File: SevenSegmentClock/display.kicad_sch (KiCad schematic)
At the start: 104 parts, among them Q1 PN2222A, Q2 PN2222A, Q3 PN2222A, Q4 PN2222A, Q5 PN2222A, Q6 PN2222A, Q7 13N50F, U1 4511, U10 4042, U11 4511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

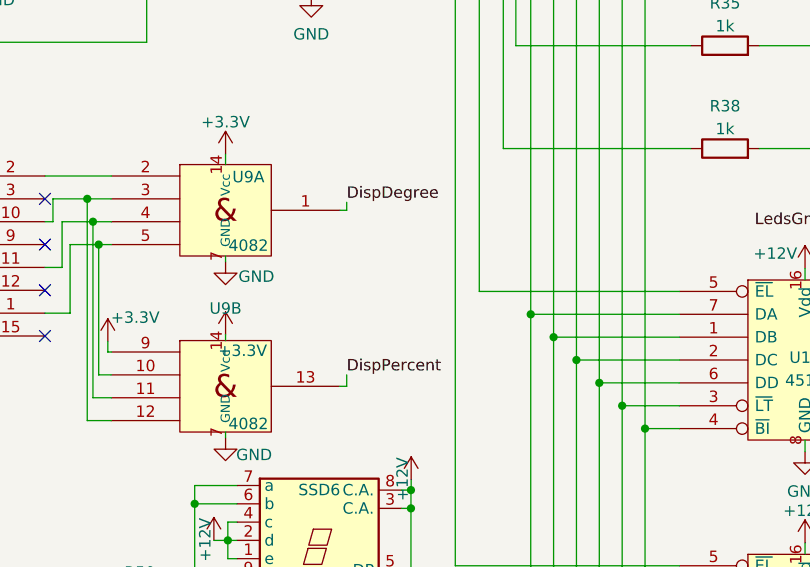
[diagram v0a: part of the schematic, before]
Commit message: Swapping around percentage and degree indicators
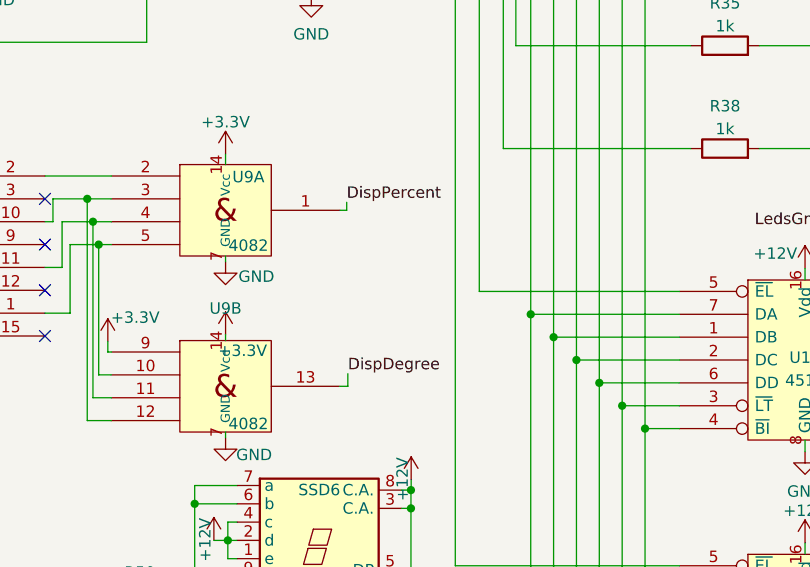
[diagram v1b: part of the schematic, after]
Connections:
- net DispDegree: now also U9.13; no longer U9.1
- net DispPercent: now also U9.1; no longer U9.13
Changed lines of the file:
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@@
-    (stroke (width 0) (type default))
-  )
-  (wire (pts (xy 91.059 203.581) (xy 91.059 202.311))
     (stroke (width 0) (type default))
   )
@@
     (stroke (width 0) (type default))
   )
+  (wire (pts (xy 91.186 203.581) (xy 91.186 202.184))
+    (stroke (width 0) (type default))
+  )
   (wire (pts (xy 114.046 25.4) (xy 114.046 57.15))
     (stroke (width 0) (type default))
@@
     (stroke (width 0) (type default))
   )
-  (wire (pts (xy 90.297 203.581) (xy 91.059 203.581))
+  (wire (pts (xy 90.297 203.581) (xy 91.186 203.581))
     (stroke (width 0) (type default))
   )
@@
     (effects (font (size 1.27 1.27)) (justify right bottom))
   )
-  (label "DispPercent" (at 91.059 202.311 0) (fields_autoplaced)
+  (label "DispPercent" (at 91.059 183.134 0) (fields_autoplaced)
     (effects (font (size 1.27 1.27)) (justify left bottom))
   )
@@
     (effects (font (size 1.27 1.27)) (justify right bottom))
   )
-  (label "DispDegree" (at 91.059 183.134 0) (fields_autoplaced)
+  (label "DispDegree" (at 91.186 202.184 0) (fields_autoplaced)
     (effects (font (size 1.27 1.27)) (justify left bottom))
   )

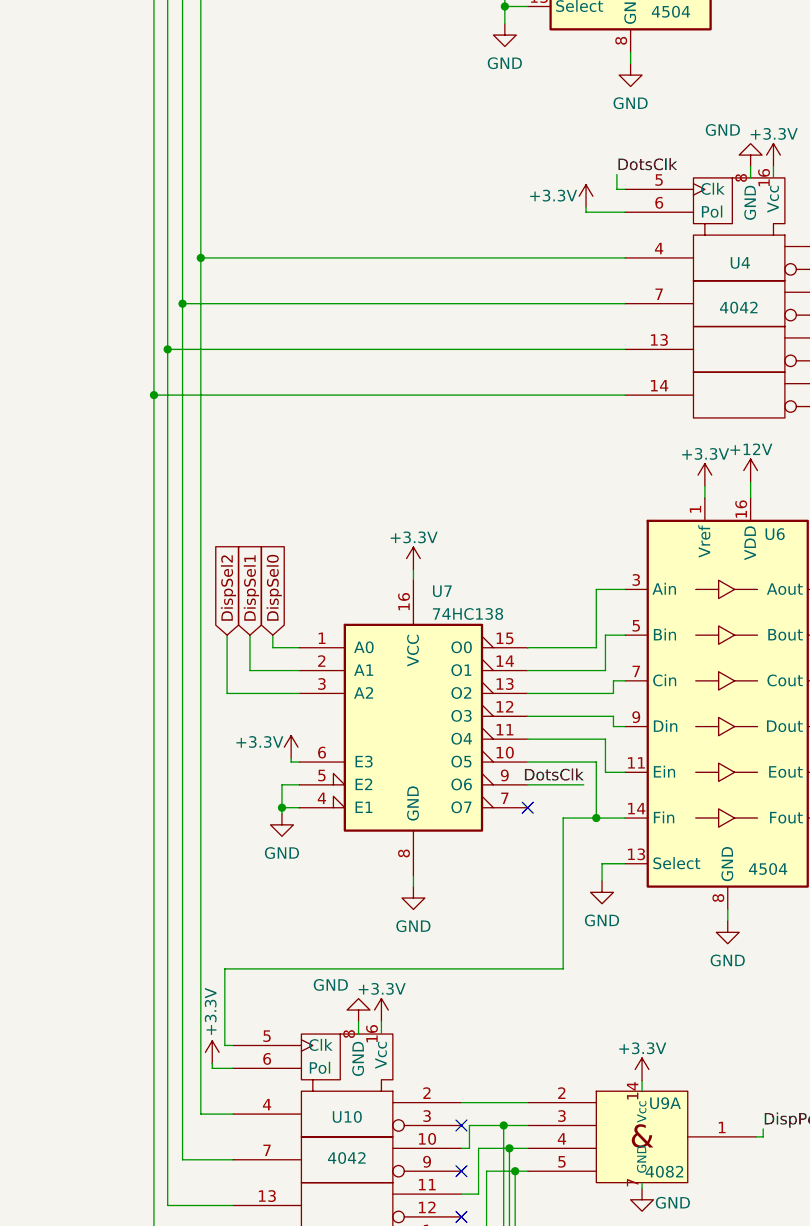
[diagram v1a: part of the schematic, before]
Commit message: Fixing the polarity of the CD4042s
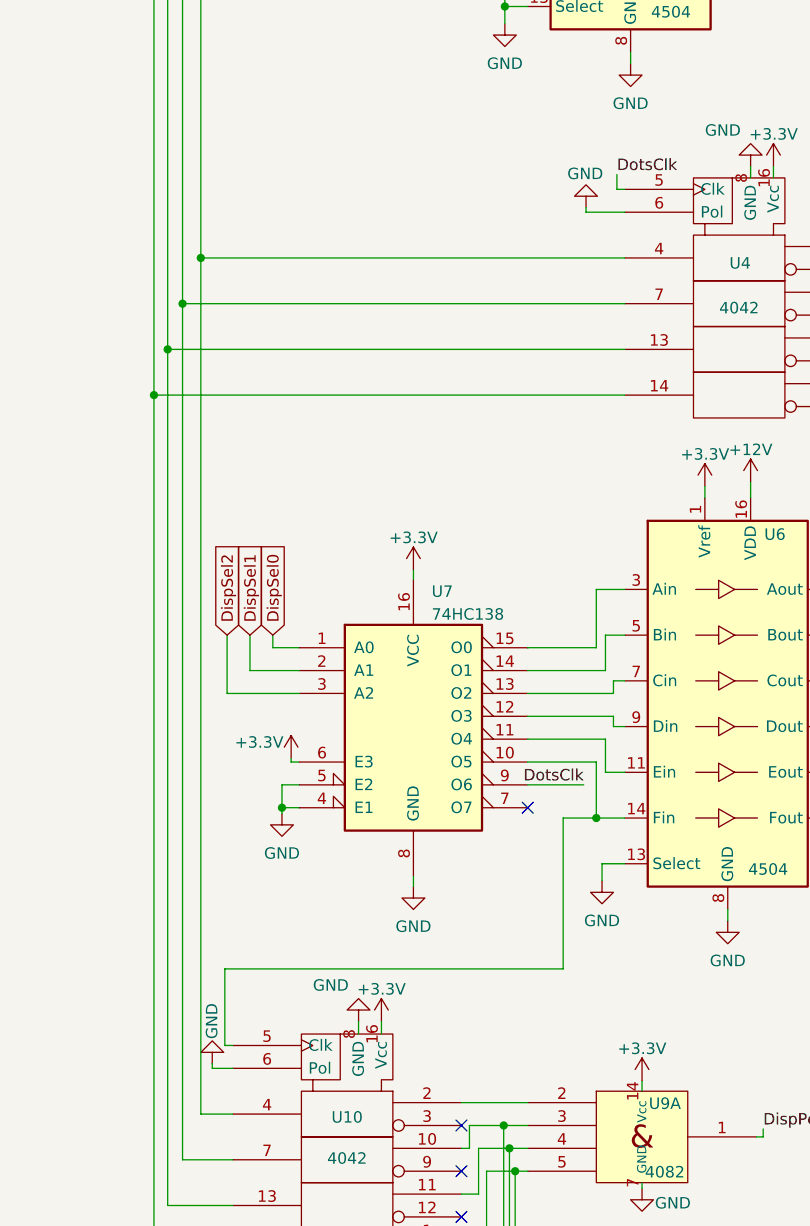
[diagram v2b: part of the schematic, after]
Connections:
- net +3.3V: no longer U10.6 (Pol), U4.6 (Pol)
- net GND: now also U10.6 (Pol), U4.6 (Pol)
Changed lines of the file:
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@@
+    )
+  )
+  (symbol (lib_id "power:GND") (at 71.374 80.772 180) (unit 1)
+    (in_bom yes) (on_board yes) (dnp no)
+    (property "Reference" "#PWR013" (at 71.374 74.422 0)
+      (effects (font (size 1.27 1.27)) hide)
+    )
+    (property "Value" "GND" (at 69.2912 77.0128 0)
+      (effects (font (size 1.27 1.27)) (justify right))
+    )
+    (property "Footprint" "" (at 71.374 80.772 0)
+      (effects (font (size 1.27 1.27)) hide)
+    )
+    (property "Datasheet" "" (at 71.374 80.772 0)
+      (effects (font (size 1.27 1.27)) hide)
+    )
+    (pin "1")
+    (instances
+      (project "SevenSegmentClock"
+        (path "/14aa22d5-bc38-4295-9b97-76c65f8b1aaa/080ade9b-5b49-48d1-8801-1844c5bd1d80"
+          (reference "#PWR013") (unit 1)
+        )
+      )
     )
   )
@@
         (path "/14aa22d5-bc38-4295-9b97-76c65f8b1aaa/080ade9b-5b49-48d1-8801-1844c5bd1d80"
           (reference "D1") (unit 1)
-        )
-      )
-    )
-  )
-  (symbol (lib_id "power:+3.3V") (at 29.845 175.895 0) (unit 1)
-    (in_bom yes) (on_board yes) (dnp no)
-    (property "Reference" "#PWR029" (at 29.845 179.705 0)
-      (effects (font (size 1.27 1.27)) hide)
-    )
-    (property "Value" "+3.3V" (at 29.718 170.1602 90)
-      (effects (font (size 1.27 1.27)))
-    )
-    (property "Footprint" "" (at 29.845 175.895 0)
-      (effects (font (size 1.27 1.27)) hide)
-    )
-    (property "Datasheet" "" (at 29.845 175.895 0)
-      (effects (font (size 1.27 1.27)) hide)
-    )
-    (pin "1")
-    (instances
-      (project "SevenSegmentClock"
-        (path "/14aa22d5-bc38-4295-9b97-76c65f8b1aaa/080ade9b-5b49-48d1-8801-1844c5bd1d80"
-          (reference "#PWR029") (unit 1)
         )
       )
@@
     )
   )
+  (symbol (lib_id "power:GND") (at 29.845 175.895 180) (unit 1)
+    (in_bom yes) (on_board yes) (dnp no)
+    (property "Reference" "#PWR029" (at 29.845 169.545 0)
+      (effects (font (size 1.27 1.27)) hide)
+    )
+    (property "Value" "GND" (at 29.8196 173.1518 90)
+      (effects (font (size 1.27 1.27)) (justify right))
+    )
+    (property "Footprint" "" (at 29.845 175.895 0)
+      (effects (font (size 1.27 1.27)) hide)
+    )
+    (property "Datasheet" "" (at 29.845 175.895 0)
+      (effects (font (size 1.27 1.27)) hide)
+    )
+    (pin "1")
+    (instances
+      (project "SevenSegmentClock"
+        (path "/14aa22d5-bc38-4295-9b97-76c65f8b1aaa/080ade9b-5b49-48d1-8801-1844c5bd1d80"
+          (reference "#PWR029") (unit 1)
+        )
+      )
+    )
+  )
   (symbol (lib_id "power:+12V") (at 184.531 164.465 0) (unit 1)
     (in_bom yes) (on_board yes) (dnp no)
@@
         )
       )
-    )
-  )
-  (symbol (lib_id "power:+3.3V") (at 71.374 80.772 0) (unit 1)
-    (in_bom yes) (on_board yes) (dnp no)
-    (property "Reference" "#PWR013" (at 71.374 84.582 0)
-      (effects (font (size 1.27 1.27)) hide)
-    )
-    (property "Value" "+3.3V" (at 67.691 79.4822 0)
-      (effects (font (size 1.27 1.27)))
-    )
-    (property "Footprint" "" (at 71.374 80.772 0)
-      (effects (font (size 1.27 1.27)) hide)
-    )
-    (property "Datasheet" "" (at 71.374 80.772 0)
-      (effects (font (size 1.27 1.27)) hide)
-    )
-    (pin "1")
-    (instances
-      (project "SevenSegmentClock"
-        (path "/14aa22d5-bc38-4295-9b97-76c65f8b1aaa/080ade9b-5b49-48d1-8801-1844c5bd1d80"
-          (reference "#PWR013") (unit 1)
-        )
-      )
